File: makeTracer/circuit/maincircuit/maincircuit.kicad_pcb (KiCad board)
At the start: 2 copper layers, 100 x 70 mm, 26 parts, among them IC1 PIC16F1778-I_SP, J1 PICKit3, J2 Sensor, J3 LED, J4 I^{2}C, J5 Motor_L, J6 Motor_R, Q1 MP4212_Q_, Q2 MP4212_Q_, SW1 SW_DPDT_x2, SW2 Reset, SW3 Red, SW4 Green, U1 74HC00

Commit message: wipp
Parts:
- removed the J3 at (108.7, 72.8)
- added R10: 10k, Resistor_THT:R_Axial_DIN0207_L6.3mm_D2.5mm_P10.16mm_Horizontal, F.Cu at (41.9, 84.1)
- added R5: 10k, Resistor_THT:R_Axial_DIN0207_L6.3mm_D2.5mm_P5.08mm_Vertical, F.Cu at (43.9, 27.0)
- added R6: 10k, Resistor_THT:R_Axial_DIN0207_L6.3mm_D2.5mm_P7.62mm_Horizontal, F.Cu at (43.9, 31.1)
- added R7: 10k, Resistor_THT:R_Axial_DIN0207_L6.3mm_D2.5mm_P10.16mm_Horizontal, F.Cu at (58.2, 36.8)
- added R8: 10k, Resistor_THT:R_Axial_DIN0207_L6.3mm_D2.5mm_P10.16mm_Horizontal, F.Cu at (41.9, 76.0)
- added R9: 10k, Resistor_THT:R_Axial_DIN0207_L6.3mm_D2.5mm_P10.16mm_Horizontal, F.Cu at (41.9, 80.0)
- added REF**: MountingHole_3.2mm_M3, MountingHole:MountingHole_3.2mm_M3, F.Cu at (115.0, 25.0)
- added REF**: MountingHole_3.2mm_M3, MountingHole:MountingHole_3.2mm_M3, F.Cu at (25.0, 85.0)
- added REF**: MountingHole_3.2mm_M3, MountingHole:MountingHole_3.2mm_M3, F.Cu at (25.0, 25.0)
- added REF**: MountingHole_3.2mm_M3, MountingHole:MountingHole_3.2mm_M3, F.Cu at (115.0, 85.0)
- added U2: 74HC595, Package_DIP:DIP-16_W7.62mm_LongPads, F.Cu at (91.4, 84.8)
- added U3: 74HC595, Package_DIP:DIP-16_W7.62mm_LongPads, F.Cu at (69.4, 84.8)
- IC1: value PIC16F1778-I_SP -> PIC16F1778-I/SP
- Q1, Q2: value MP4212_Q_ -> MP4212; footprint mylibrary:MP4212_Q_WIDE -> D4jikkenLibrary:MP4212_WIDE
- moved SW4 5.53 mm to (66.2, 28.0)
- moved IC1 4.29 mm to (105.5, 51.2)
- moved C1 4.28 mm to (85.2, 62.0)
- moved J1 4.28 mm to (116.8, 60.2)
- moved J2 4.28 mm to (93.0, 46.5)
- moved J3 4.28 mm to (96.0, 66.5)
- moved LS1 4.28 mm to (83.9, 42.5)
- moved R1 4.28 mm to (92.6, 41.2)
- moved SW2 4.28 mm to (90.0, 28.0)
- moved SW3 4.28 mm to (77.5, 28.0)
- moved Q1 1.25 mm to (31.2, 47.0)
- moved Q2 1.25 mm to (31.2, 86.0)
- moved C5 0.76 mm to (37.8, 63.2)
- moved C4 0.75 mm to (37.8, 24.0)
- moved J6 0.60 mm to (23.0, 76.9)
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- renumbered J4 to J3
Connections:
- IC1 pad 22: LED_SREG_DAT -> /16x2LEDs/Data
- IC1 pad 23: LED_SREG_CLK -> /16x2LEDs/Clock
- IC1 pad 24: LED_SREG_SEND -> /16x2LEDs/Flash
- IC1 pad 25: LED_SELG -> unconnected-(IC1-RB4-Pad25)
- IC1 pad 26: LED_SELR -> unconnected-(IC1-RB5-Pad26)
- SW1 pad : GND -> (no net)
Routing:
- net /Motordrive/R_SEL2: track 66.5 -> 23.0 mm
- net /Motordrive/R_SEL1: track 86.6 -> 65.0 mm
- net Net-(Q2-G_4): track 32.1 -> 19.7 mm
- net Net-(Q2-S_3): track 12.0 -> 0.00 mm
- net /Motordrive/L_SEL2: track 51.9 -> 42.0 mm
- net Net-(Q2-G_3): track 40.1 -> 31.2 mm
- net VDD: track 133.5 -> 142.1 mm, vias 2 -> 4
- net GND: track 11.7 -> 3.22 mm
- net /Motordrive/L_PWM: track 22.6 -> 14.3 mm
- net PICKit3_MCLR: track 42.4 -> 35.9 mm
- net /Motordrive/L_SEL1: track 69.0 -> 62.7 mm
- net Net-(J6-Pin_2): track 22.6 -> 28.6 mm
- net Net-(J6-Pin_1): track 25.1 -> 27.6 mm
- net Net-(J5-Pin_2): track 21.7 -> 24.0 mm
- net PICKit3_ICSPDAT: track 15.0 -> 13.5 mm
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
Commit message: done: maincircuit
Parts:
- added C6: 0.1u_pass, Capacitor_THT:C_Disc_D5.0mm_W2.5mm_P2.50mm, F.Cu at (112.7, 80.0)
- added C7: 0.1u_pass, Capacitor_THT:C_Disc_D5.0mm_W2.5mm_P2.50mm, F.Cu at (87.7, 57.9)
- added LED1: Circle, LED_THT:LED_D3.0mm-3, F.Cu at (85.0, 83.0)
- added LED10: Circle, LED_THT:LED_D3.0mm-3, F.Cu at (79.5, 56.0)
- added LED11: Circle, LED_THT:LED_D3.0mm-3, F.Cu at (75.0, 59.0)
- added LED12: Circle, LED_THT:LED_D3.0mm-3, F.Cu at (72.0, 63.5)
- added LED13: Circle, LED_THT:LED_D3.0mm-3, F.Cu at (71.0, 69.0)
- added LED14: Circle, LED_THT:LED_D3.0mm-3, F.Cu at (72.0, 74.5)
- added LED15: Circle, LED_THT:LED_D3.0mm-3, F.Cu at (75.0, 79.0)
- added LED16: Circle, LED_THT:LED_D3.0mm-3, F.Cu at (79.5, 82.0)
- added LED2: Circle, LED_THT:LED_D3.0mm-3, F.Cu at (90.5, 82.0)
- added LED3: Circle, LED_THT:LED_D3.0mm-3, F.Cu at (95.0, 79.0)
- added LED4: Circle, LED_THT:LED_D3.0mm-3, F.Cu at (98.0, 74.5)
- added LED5: Circle, LED_THT:LED_D3.0mm-3, F.Cu at (99.0, 69.0)
- added LED6: Circle, LED_THT:LED_D3.0mm-3, F.Cu at (98.0, 63.5)
- added LED7: Circle, LED_THT:LED_D3.0mm-3, F.Cu at (95.0, 59.0)
- added LED8: Circle, LED_THT:LED_D3.0mm-3, F.Cu at (90.5, 56.0)
- added LED9: Circle, LED_THT:LED_D3.0mm-3, F.Cu at (85.0, 55.0)
- added P1: FrontsidePort, Connector_PinHeader_2.54mm:PinHeader_1x02_P2.54mm_Vertical, F.Cu at (56.8, 81.5)
- added R11: 470, Resistor_THT:R_Axial_DIN0207_L6.3mm_D2.5mm_P2.54mm_Vertical, F.Cu at (106.4, 88.5)
- added R12: 470, Resistor_THT:R_Axial_DIN0207_L6.3mm_D2.5mm_P15.24mm_Horizontal, F.Cu at (107.0, 75.4)
- added R13: 470, Resistor_THT:R_Axial_DIN0207_L6.3mm_D2.5mm_P2.54mm_Vertical, F.Cu at (94.6, 75.5)
- added R14: 470, Resistor_THT:R_Axial_DIN0207_L6.3mm_D2.5mm_P2.54mm_Vertical, F.Cu at (94.6, 71.5)
- added R15: 470, Resistor_THT:R_Axial_DIN0207_L6.3mm_D2.5mm_P2.54mm_Vertical, F.Cu at (94.6, 67.5)
- added R16: 470, Resistor_THT:R_Axial_DIN0207_L6.3mm_D2.5mm_P2.54mm_Vertical, F.Cu at (94.6, 63.5)
- added R17: 470, Resistor_THT:R_Axial_DIN0207_L6.3mm_D2.5mm_P2.54mm_Vertical, F.Cu at (104.8, 57.5)
- added R18: 470, Resistor_THT:R_Axial_DIN0207_L6.3mm_D2.5mm_P2.54mm_Vertical, F.Cu at (104.8, 54.5)
- added R19: 470, Resistor_THT:R_Axial_DIN0207_L6.3mm_D2.5mm_P2.54mm_Vertical, F.Cu at (78.0, 60.1)
- added R20: 470, Resistor_THT:R_Axial_DIN0207_L6.3mm_D2.5mm_P2.54mm_Vertical, F.Cu at (75.0, 65.4)
- added R21: 470, Resistor_THT:R_Axial_DIN0207_L6.3mm_D2.5mm_P2.54mm_Vertical, F.Cu at (75.0, 68.4)
- added R22: 470, Resistor_THT:R_Axial_DIN0207_L6.3mm_D2.5mm_P2.54mm_Vertical, F.Cu at (75.0, 71.4)
- added R23: 470, Resistor_THT:R_Axial_DIN0207_L6.3mm_D2.5mm_P2.54mm_Vertical, F.Cu at (75.0, 74.4)
- added R24: 470, Resistor_THT:R_Axial_DIN0207_L6.3mm_D2.5mm_P2.54mm_Vertical, F.Cu at (67.4, 80.6)
- added R25: 470, Resistor_THT:R_Axial_DIN0207_L6.3mm_D2.5mm_P2.54mm_Vertical, F.Cu at (67.4, 85.8)
- added R26: 470, Resistor_THT:R_Axial_DIN0207_L6.3mm_D2.5mm_P2.54mm_Vertical, F.Cu at (72.7, 88.3)
- added Tr1: DTC114E, Package_TO_SOT_THT:TO-92, F.Cu at (46.6, 80.1)
- added Tr2: DTC114E, Package_TO_SOT_THT:TO-92, F.Cu at (52.6, 77.3)
- PWR1: renamed from D1; value LED_Dual_AKA -> PowerIndicator
- Q2: moved to B.Cu
- R1: footprint Resistor_THT:R_Axial_DIN0207_L6.3mm_D2.5mm_P10.16mm_Horizontal -> Resistor_THT:R_Axial_DIN0207_L6.3mm_D2.5mm_P2.54mm_Vertical
- R10, R8: footprint Resistor_THT:R_Axial_DIN0207_L6.3mm_D2.5mm_P10.16mm_Horizontal -> Resistor_THT:R_Axial_DIN0207_L6.3mm_D2.5mm_P15.24mm_Horizontal
- R6: footprint Resistor_THT:R_Axial_DIN0207_L6.3mm_D2.5mm_P7.62mm_Horizontal -> Resistor_THT:R_Axial_DIN0207_L6.3mm_D2.5mm_P10.16mm_Horizontal
- R7: footprint Resistor_THT:R_Axial_DIN0207_L6.3mm_D2.5mm_P10.16mm_Horizontal -> Resistor_THT:R_Axial_DIN0207_L6.3mm_D2.5mm_P7.62mm_Horizontal
- R9: footprint Resistor_THT:R_Axial_DIN0207_L6.3mm_D2.5mm_P10.16mm_Horizontal -> Resistor_THT:R_Axial_DIN0207_L6.3mm_D2.5mm_P5.08mm_Vertical
- moved J3 53.5 mm to (57.0, 29.9), turned to 90 degrees
- moved LS1 39.3 mm to (46.0, 32.1), turned to 90 degrees
- moved R9 35.5 mm to (64.0, 52.3), turned to 90 degrees
- moved U2 31.8 mm to (110.2, 59.1), turned to 0 degrees
- moved R6 31.4 mm to (61.0, 57.4), turned to 90 degrees
- moved U3 26.4 mm to (81.2, 61.2), turned to 0 degrees
- moved C1 17.6 mm to (76.2, 46.9)
- moved IC1 17.5 mm to (96.5, 36.2)
- moved J2 17.5 mm to (84.0, 31.5)
- moved SW2 15.7 mm to (104.2, 34.5), turned to -90 degrees
- moved R7 15.0 mm to (43.5, 39.8), turned to -90 degrees
- moved R5 14.5 mm to (46.8, 41.2), turned to -90 degrees
- moved R10 13.9 mm to (42.5, 70.2)
- moved J1 10.8 mm to (113.5, 50.0), turned to 180 degrees
- moved R1 10.5 mm to (102.0, 46.0), turned to 180 degrees
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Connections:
- IC1 pad 25: unconnected-(IC1-RB4-Pad25) -> /16x2LEDs/Select_Red
- IC1 pad 26: unconnected-(IC1-RB5-Pad26) -> /16x2LEDs/Select_Green
- U2 pad 10: /16x2LEDs/~{Clear} -> VDD
- U2 pad 13: /16x2LEDs/~{Enable} -> GND
- U3 pad 10: /16x2LEDs/~{Clear} -> VDD
- U3 pad 13: /16x2LEDs/~{Enable} -> GND
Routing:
- net VDD: track 142.1 -> 373.7 mm, vias 4 -> 8
- net /16x2LEDs/Green_Src: track 0.00 -> 138.3 mm
- net GND: track 3.22 -> 135.4 mm, vias 0 -> 26
- net /16x2LEDs/Red_Src: track 0.00 -> 122.3 mm
- net /16x2LEDs/Clock: track 0.00 -> 102.8 mm, vias 0 -> 8
- net /16x2LEDs/Flash: track 0.00 -> 78.7 mm, vias 0 -> 6
- net /16x2LEDs/Select_Red: track 0.00 -> 69.3 mm, vias 0 -> 4
- net Net-(U2-QH'): track 0.00 -> 68.5 mm
- net /16x2LEDs/Select_Green: track 0.00 -> 62.0 mm, vias 0 -> 2
- net /Motordrive/R_SEL2: track 23.0 -> 83.7 mm, vias 2 -> 6
- net /16x2LEDs/Data: track 0.00 -> 47.4 mm
- net I^{2}C_SDA: track 0.00 -> 45.0 mm, vias 0 -> 4
- net /16x2LEDs/LED1: track 0.00 -> 38.8 mm
- net /Motordrive/R_PWM: track 10.3 -> 47.8 mm, vias 1 -> 4
- net /16x2LEDs/LED3: track 0.00 -> 35.1 mm, vias 0 -> 2
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- added copper zone on B.Cu, net GND
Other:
- board text added: "1"
- board text added: "QC Pass"

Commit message: fix: yabai jumper
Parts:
- added REF**: KiCad-Logo2_8mm_SilkScreen, Symbol:KiCad-Logo2_8mm_SilkScreen, B.Cu at (52.0, 78.9)
- BT1: footprint Connector_PinHeader_2.54mm:PinHeader_1x02_P2.54mm_Horizontal -> Connector_PinHeader_2.54mm:PinHeader_1x02_P2.54mm_Vertical
- R10, R12, R8: footprint Resistor_THT:R_Axial_DIN0207_L6.3mm_D2.5mm_P15.24mm_Horizontal -> Resistor_THT:R_Axial_DIN0207_L6.3mm_D2.5mm_P7.62mm_Horizontal
- R11, R13, R14, R15, R16, R17, R18, R19, R20, R21, R22, R23, R24, R25, R26: footprint Resistor_THT:R_Axial_DIN0207_L6.3mm_D2.5mm_P2.54mm_Vertical -> Resistor_THT:R_Axial_DIN0207_L6.3mm_D2.5mm_P7.62mm_Horizontal
- R2: footprint Resistor_THT:R_Axial_DIN0207_L6.3mm_D2.5mm_P2.54mm_Vertical -> Resistor_THT:R_Axial_DIN0207_L6.3mm_D2.5mm_P5.08mm_Vertical
- R3: footprint Resistor_THT:R_Axial_DIN0309_L9.0mm_D3.2mm_P12.70mm_Horizontal -> Resistor_THT:R_Axial_DIN0309_L9.0mm_D3.2mm_P20.32mm_Horizontal
- R5: footprint Resistor_THT:R_Axial_DIN0207_L6.3mm_D2.5mm_P5.08mm_Vertical -> Resistor_THT:R_Axial_DIN0207_L6.3mm_D2.5mm_P7.62mm_Horizontal
- R7: footprint Resistor_THT:R_Axial_DIN0207_L6.3mm_D2.5mm_P7.62mm_Horizontal -> Resistor_THT:R_Axial_DIN0207_L6.3mm_D2.5mm_P10.16mm_Horizontal
- R9: footprint Resistor_THT:R_Axial_DIN0207_L6.3mm_D2.5mm_P5.08mm_Vertical -> Resistor_THT:R_Axial_DIN0207_L6.3mm_D2.5mm_P2.54mm_Vertical
- moved Tr2 75.9 mm to (124.7, 53.8), turned to 0 degrees
- moved Tr1 75.8 mm to (119.2, 58.5), turned to 0 degrees
- moved P1 72.7 mm to (125.5, 57.9), turned to 90 degrees
- moved J3 72.3 mm to (127.5, 45.9), turned to 180 degrees
- moved C6 20.3 mm to (126.2, 64.9)
- moved R2 18.5 mm to (23.1, 42.6), turned to 90 degrees
- moved PWR1 18.4 mm to (22.6, 46.4), turned to 0 degrees
- moved U2 18.1 mm to (125.9, 68.1), turned to -90 degrees
- moved R20 17.6 mm to (64.0, 51.6), turned to -90 degrees
- moved J1 17.3 mm to (125.3, 37.4), turned to -90 degrees
- moved R1 16.2 mm to (100.0, 29.9), turned to 90 degrees
- moved R23 15.5 mm to (60.0, 70.3), turned to -90 degrees
- moved R12 13.1 mm to (101.8, 87.5), turned to 45 degrees
- moved R11 13.0 mm to (115.2, 78.9)
- moved R19 11.2 mm to (72.7, 50.2)
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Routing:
- net /16x2LEDs/Flash: track 78.7 -> 124.7 mm, vias 6 -> 0
- net /16x2LEDs/LED1: track 38.8 -> 3.36 mm
- net /16x2LEDs/Select_Red: track 69.3 -> 36.8 mm, vias 4 -> 0
- net Net-(U2-QH'): track 68.5 -> 37.0 mm
- net /16x2LEDs/Data: track 47.4 -> 78.0 mm
- net GND: track 135.4 -> 106.5 mm, vias 26 -> 28
- net /16x2LEDs/LED13: track 7.10 -> 35.9 mm
- net /16x2LEDs/LED2: track 3.61 -> 29.6 mm
- net /16x2LEDs/Clock: track 102.8 -> 77.1 mm, vias 8 -> 2
- net /16x2LEDs/Select_Green: track 62.0 -> 39.9 mm, vias 2 -> 0
- net /16x2LEDs/LED6: track 26.2 -> 4.24 mm
- net I^{2}C_SCL: track 34.5 -> 54.9 mm
- net /16x2LEDs/Green_Src: track 138.3 -> 158.6 mm
- net /16x2LEDs/LED10: track 5.70 -> 22.3 mm
- net Net-(LED2-K): track 27.7 -> 11.6 mm
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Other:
- board size 100 x 70 mm -> 110 x 70 mm
- board text added: "Front"
- board text added: "PICKit3 Size"

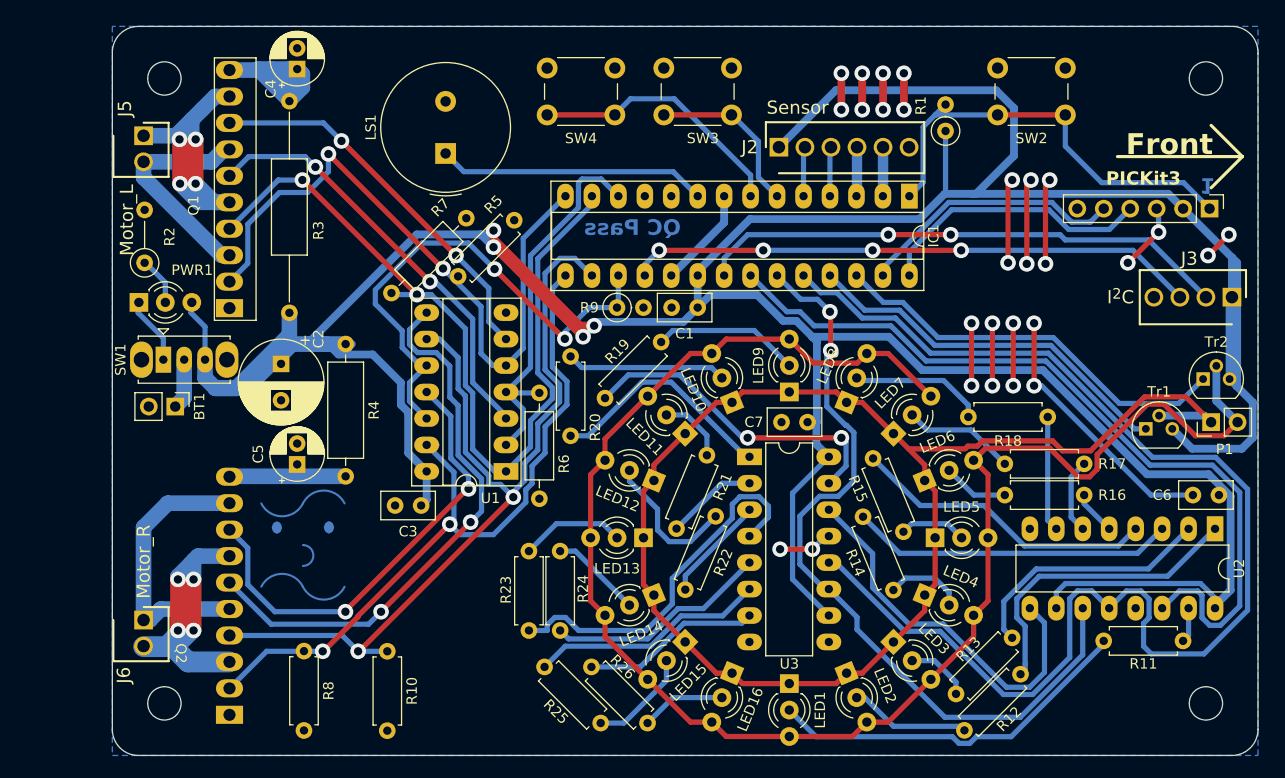
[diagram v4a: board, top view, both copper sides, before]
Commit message: fix: .2mm to .4mm
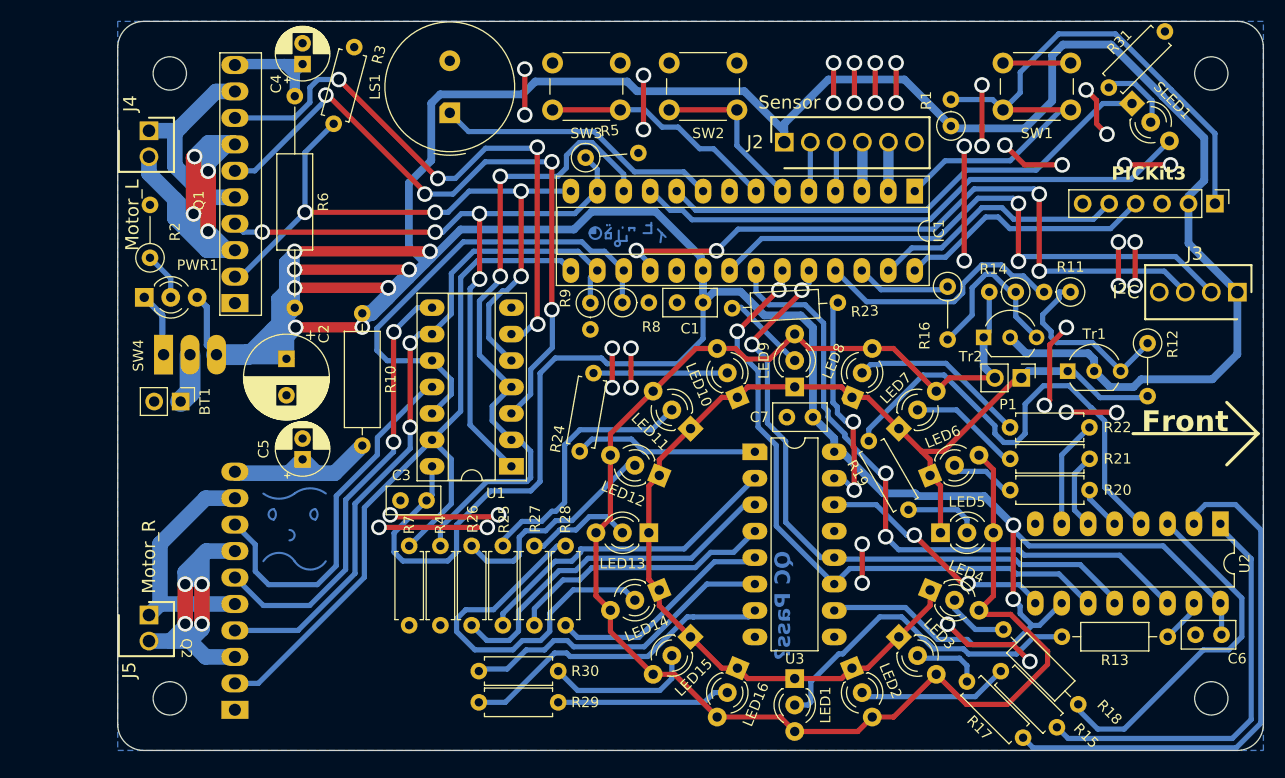
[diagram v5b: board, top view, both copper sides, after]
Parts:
- added R11: 10k, Resistor_THT:R_Axial_DIN0207_L6.3mm_D2.5mm_P2.54mm_Vertical, F.Cu at (112.0, 45.4)
- added R12: 10k, Resistor_THT:R_Axial_DIN0207_L6.3mm_D2.5mm_P5.08mm_Vertical, F.Cu at (119.4, 50.3)
- added R14: 10k, Resistor_THT:R_Axial_DIN0207_L6.3mm_D2.5mm_P2.54mm_Vertical, F.Cu at (106.7, 45.4)
- added R16: 10k, Resistor_THT:R_Axial_DIN0207_L6.3mm_D2.5mm_P5.08mm_Vertical, F.Cu at (100.2, 44.9)
- added R31: 470, Resistor_THT:R_Axial_DIN0207_L6.3mm_D2.5mm_P7.62mm_Horizontal, F.Cu at (115.7, 25.8)
- added SLED1: StatusLED, LED_THT:LED_D3.0mm-3, F.Cu at (117.9, 27.3)
- R13: renamed from R11; footprint Resistor_THT:R_Axial_DIN0207_L6.3mm_D2.5mm_P7.62mm_Horizontal -> Resistor_THT:R_Axial_DIN0207_L6.3mm_D2.5mm_P10.16mm_Horizontal
- R18: renamed from R14; footprint Resistor_THT:R_Axial_DIN0207_L6.3mm_D2.5mm_P7.62mm_Horizontal -> Resistor_THT:R_Axial_DIN0207_L6.3mm_D2.5mm_P10.16mm_Horizontal
- R2: value 1k -> 470
- R23: renamed from R19; footprint Resistor_THT:R_Axial_DIN0207_L6.3mm_D2.5mm_P7.62mm_Horizontal -> Resistor_THT:R_Axial_DIN0207_L6.3mm_D2.5mm_P10.16mm_Horizontal
- R4: renamed from R6; footprint Resistor_THT:R_Axial_DIN0207_L6.3mm_D2.5mm_P10.16mm_Horizontal -> Resistor_THT:R_Axial_DIN0207_L6.3mm_D2.5mm_P7.62mm_Horizontal
- R5: renamed from R7; footprint Resistor_THT:R_Axial_DIN0207_L6.3mm_D2.5mm_P10.16mm_Horizontal -> Resistor_THT:R_Axial_DIN0207_L6.3mm_D2.5mm_P5.08mm_Vertical
- R9: renamed from R10; footprint Resistor_THT:R_Axial_DIN0207_L6.3mm_D2.5mm_P7.62mm_Horizontal -> Resistor_THT:R_Axial_DIN0207_L6.3mm_D2.5mm_P2.54mm_Vertical
- SW4: renamed from SW1; footprint Button_Switch_THT:SW_Slide_1P2T_CK_OS102011MS2Q -> D4jikkenLibrary:ToggleSW_3pin
- Tr1, Tr2: value DTC114E -> 2SC1815; footprint Package_TO_SOT_THT:TO-92 -> Package_TO_SOT_THT:TO-92_Inline_Wide
- moved R9 38.7 mm to (65.9, 46.5)
- moved R26 23.6 mm to (54.5, 69.8), turned to -90 degrees
- moved R5 22.7 mm to (65.4, 32.5), turned to 5 degrees
- moved Tr2 21.4 mm to (103.7, 49.8)
- moved R25 21.4 mm to (57.5, 69.8), turned to -90 degrees
- moved R3 18.9 mm to (41.2, 29.2), turned to 75 degrees
- moved P1 18.7 mm to (107.3, 53.6), turned to -90 degrees
- moved R4 17.5 mm to (51.5, 69.8)
- moved R7 14.3 mm to (48.5, 69.8)
- moved C6 13.4 mm to (126.5, 78.3)
- moved R18 11.2 mm to (105.6, 77.8), turned to -45 degrees
- moved Tr1 9.32 mm to (111.7, 53.0)
- moved R30 8.81 mm to (62.8, 84.8), turned to 180 degrees
- moved R23 7.55 mm to (79.5, 47.0), turned to 3 degrees
- moved R15 6.67 mm to (105.3, 81.8), turned to -45 degrees
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- renumbered J5 to J4, J6 to J5, R4 to R10, R12 to R15, R13 to R17, R15 to R19, R16 to R20, R17 to R21, R18 to R22, R20 to R24, R21 to R25, R22 to R26, R23 to R27, R24 to R28, R25 to R29, R5 to R3, R26 to R30, R3 to R6, R8 to R7, R9 to R8, SW2 to SW1, SW3 to SW2, SW4 to SW3
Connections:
- IC1 pad 10: unconnected-(IC1-RA6-Pad10) -> Net-(IC1-RA6)
- IC1 pad 11: unconnected-(IC1-RC0-Pad11) -> Net-(IC1-RC0)
- Tr1 pad 1: /16x2LEDs/Select_Red -> /16x2LEDs/Red_Src
- Tr1 pad 2: /16x2LEDs/Red_Src -> VDD
- Tr1 pad 3: VDD -> Net-(Tr1-B)
- Tr2 pad 1: /16x2LEDs/Select_Green -> /16x2LEDs/Green_Src
- Tr2 pad 2: /16x2LEDs/Green_Src -> VDD
- Tr2 pad 3: VDD -> Net-(Tr2-B)
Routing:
- net VDD: track 387.2 -> 471.4 mm, vias 4 -> 10
- net /16x2LEDs/Flash: track 124.7 -> 62.8 mm, vias 0 -> 2
- net Net-(IC1-RC0): track 0.00 -> 54.1 mm
- net Net-(IC1-RA6): track 0.00 -> 48.7 mm
- net /16x2LEDs/Select_Green: track 39.9 -> 9.13 mm
- net Net-(LED14-K): track 8.80 -> 36.2 mm
- net /16x2LEDs/LED3: track 24.5 -> 51.4 mm
- net /Motordrive/L_PWM: track 37.6 -> 62.9 mm, vias 0 -> 2
- net /16x2LEDs/LED12: track 10.2 -> 34.3 mm
- net Net-(Q1-G_3): track 41.4 -> 64.8 mm, vias 2 -> 4
- net /16x2LEDs/LED11: track 8.81 -> 30.9 mm
- net PICKit3_MCLR: track 43.3 -> 65.3 mm
- net GND: track 106.5 -> 127.4 mm, vias 28 -> 42
- net /Motordrive/R_SEL1: track 86.7 -> 66.2 mm
- net Net-(J4-Pin_2): track 21.6 -> 41.8 mm, vias 0 -> 4
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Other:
- board text added: "QC Pass?"
- board text removed: "1"
- board text removed: "QC Pass"
